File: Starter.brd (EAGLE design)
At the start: 44.1 x 26.7 mm, 9 parts, among them IC1 LM317MBSTT3

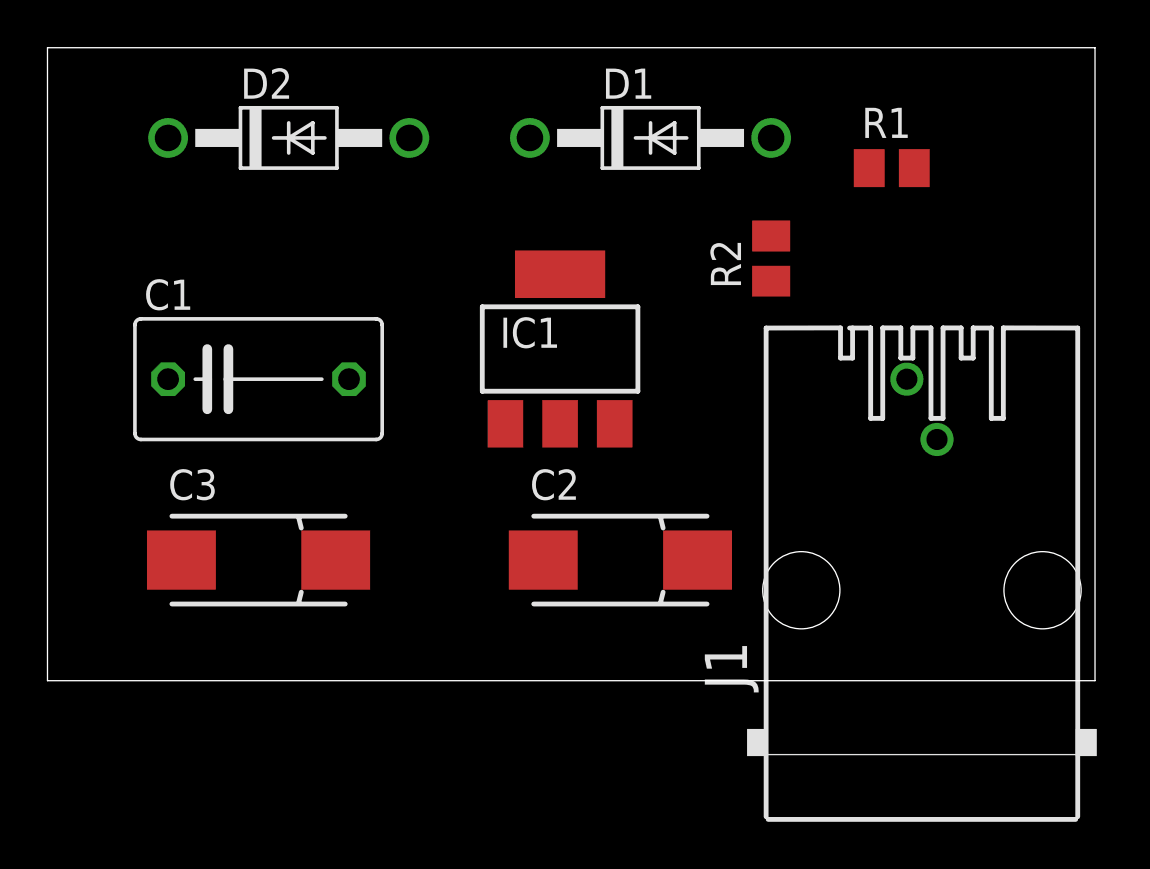
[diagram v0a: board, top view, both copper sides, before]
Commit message: Copper poured
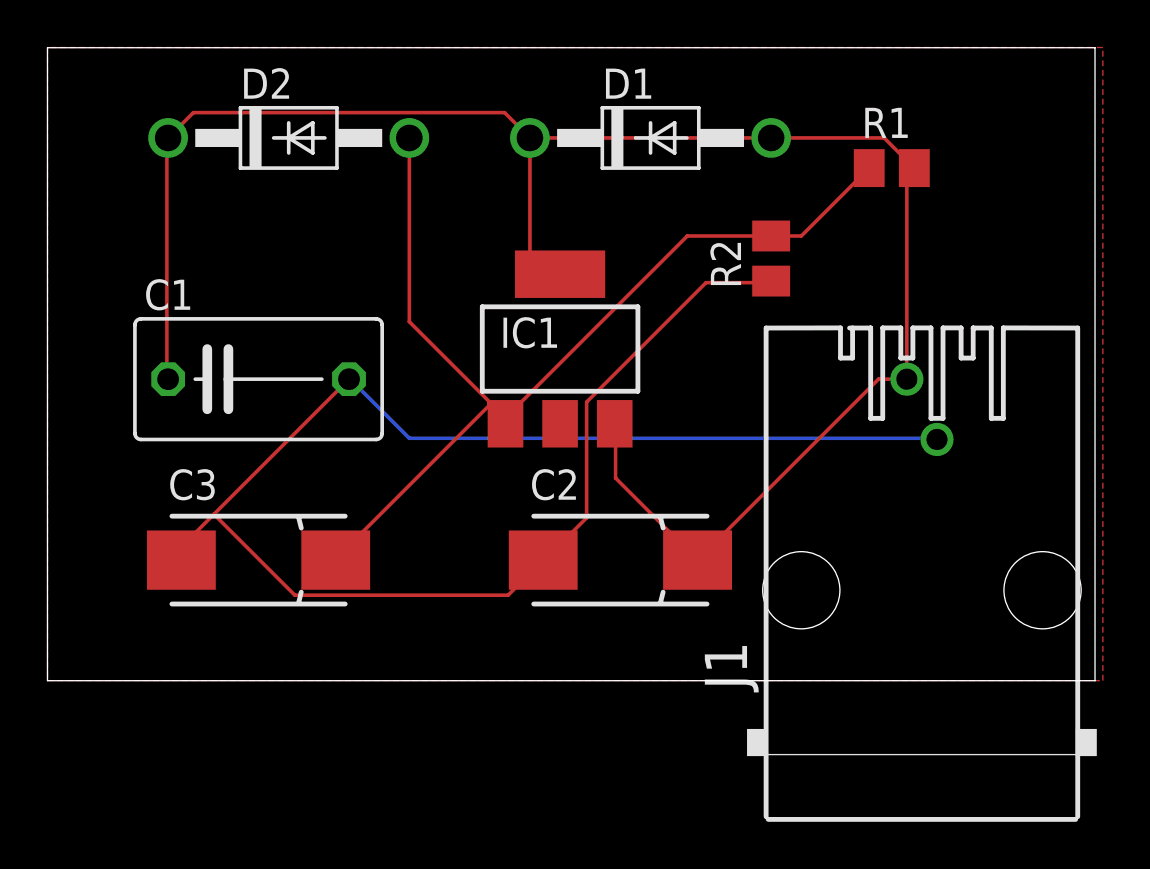
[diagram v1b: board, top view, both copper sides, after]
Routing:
- net +5V: track 0.00 -> 78.0 mm
- net GND: track 0.00 -> 69.6 mm
- net N$1: track 0.00 -> 43.9 mm
- added copper zone on layer 1, net GND
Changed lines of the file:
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@@
 <drawing>
 <settings>
-<setting alwaysvectorfont="no"/>
+<setting alwaysvectorfont="yes"/>
 <setting verticaltext="up"/>
 </settings>
@@
 <contactref element="C2" pad="-"/>
 <contactref element="J1" pad="2"/>
-<wire x1="20.88" y1="5.08" x2="30.48" y2="16.83" width="0" layer="19" extent="1-1"/>
-<wire x1="12.7" y1="12.7" x2="20.88" y2="5.08" width="0" layer="19" extent="1-1"/>
-<wire x1="5.64" y1="5.08" x2="12.7" y2="12.7" width="0" layer="19" extent="1-1"/>
-<wire x1="37.465" y1="10.16" x2="5.64" y2="5.08" width="0" layer="19" extent="1-1"/>
+<wire x1="27.7368" y1="16.764" x2="30.48" y2="16.764" width="0.1524" layer="1"/>
+<wire x1="22.7076" y1="11.7348" x2="27.7368" y2="16.764" width="0.1524" layer="1"/>
+<wire x1="22.7076" y1="6.858" x2="22.7076" y2="11.7348" width="0.1524" layer="1"/>
+<wire x1="21.0312" y1="5.1816" x2="22.7076" y2="6.858" width="0.1524" layer="1"/>
+<wire x1="30.48" y1="16.764" x2="30.48" y2="16.83" width="0.1524" layer="1"/>
+<wire x1="21.0312" y1="5.1816" x2="20.88" y2="5.08" width="0.1524" layer="1"/>
+<wire x1="15.24" y1="10.2108" x2="37.338" y2="10.2108" width="0.1524" layer="16"/>
+<wire x1="12.8016" y1="12.6492" x2="15.24" y2="10.2108" width="0.1524" layer="16"/>
+<wire x1="37.338" y1="10.2108" x2="37.465" y2="10.16" width="0.1524" layer="16"/>
+<wire x1="12.8016" y1="12.6492" x2="12.7" y2="12.7" width="0.1524" layer="16"/>
+<wire x1="5.7912" y1="5.7912" x2="5.7912" y2="5.1816" width="0.1524" layer="1"/>
+<wire x1="12.7" y1="12.7" x2="7.0104" y2="7.0104" width="0.1524" layer="1"/>
+<wire x1="7.0104" y1="7.0104" x2="5.7912" y2="5.7912" width="0.1524" layer="1"/>
+<wire x1="5.7912" y1="5.1816" x2="5.64" y2="5.08" width="0.1524" layer="1"/>
+<wire x1="7.0104" y1="7.0104" x2="10.4194" y2="3.6014" width="0.1524" layer="1"/>
+<wire x1="10.4194" y1="3.6014" x2="19.4014" y2="3.6014" width="0.1524" layer="1"/>
+<wire x1="19.4014" y1="3.6014" x2="20.88" y2="5.08" width="0.1524" layer="1"/>
+<polygon width="0.1524" layer="1">
+<vertex x="0" y="26.67"/>
+<vertex x="0" y="0"/>
+<vertex x="44.45" y="0"/>
+<vertex x="44.45" y="26.67"/>
+</polygon>
 </signal>
 <signal name="N$1">
@@
 <contactref element="R2" pad="2"/>
 <contactref element="C3" pad="+"/>
-<wire x1="30.48" y1="18.73" x2="34.61" y2="21.59" width="0" layer="19" extent="1-1"/>
-<wire x1="19.29" y1="10.82" x2="30.48" y2="18.73" width="0" layer="19" extent="1-1"/>
-<wire x1="12.14" y1="5.08" x2="19.29" y2="10.82" width="0" layer="19" extent="1-1"/>
-<wire x1="15.24" y1="22.86" x2="19.29" y2="10.82" width="0" layer="19" extent="1-1"/>
+<wire x1="30.48" y1="18.73" x2="26.95" y2="18.73" width="0.1524" layer="1"/>
+<wire x1="26.95" y1="18.73" x2="19.29" y2="11.07" width="0.1524" layer="1"/>
+<wire x1="15.24" y1="22.86" x2="15.24" y2="15.12" width="0.1524" layer="1"/>
+<wire x1="15.24" y1="15.12" x2="19.29" y2="11.07" width="0.1524" layer="1"/>
+<wire x1="19.29" y1="11.07" x2="19.29" y2="10.82" width="0.1524" layer="1"/>
+<wire x1="18.5928" y1="11.5824" x2="12.192" y2="5.1816" width="0.1524" layer="1"/>
+<wire x1="18.5928" y1="11.7348" x2="18.5928" y2="11.5824" width="0.1524" layer="1"/>
+<wire x1="12.192" y1="5.1816" x2="12.14" y2="5.08" width="0.1524" layer="1"/>
+<wire x1="18.5928" y1="11.7348" x2="19.29" y2="10.82" width="0.1524" layer="1"/>
+<wire x1="30.48" y1="18.73" x2="31.75" y2="18.73" width="0.1524" layer="1"/>
+<wire x1="31.75" y1="18.73" x2="34.61" y2="21.59" width="0.1524" layer="1"/>
 </signal>
 <signal name="+5V">
@@
 <contactref element="D1" pad="C"/>
 <contactref element="J1" pad="1"/>
-<wire x1="30.48" y1="22.86" x2="36.51" y2="21.59" width="0" layer="19" extent="1-1"/>
-<wire x1="20.32" y1="22.86" x2="30.48" y2="22.86" width="0" layer="19" extent="1-1"/>
-<wire x1="21.59" y1="17.12" x2="20.32" y2="22.86" width="0" layer="19" extent="1-1"/>
-<wire x1="23.89" y1="10.82" x2="21.59" y2="17.12" width="0" layer="19" extent="1-1"/>
-<wire x1="27.38" y1="5.08" x2="23.89" y2="10.82" width="0" layer="19" extent="1-1"/>
-<wire x1="5.08" y1="22.86" x2="20.32" y2="22.86" width="0" layer="19" extent="1-1"/>
-<wire x1="5.08" y1="12.7" x2="5.08" y2="22.86" width="0" layer="19" extent="1-1"/>
-<wire x1="36.195" y1="12.7" x2="5.08" y2="22.86" width="0" layer="19" extent="1-1"/>
+<wire x1="36.51" y1="21.59" x2="36.195" y2="21.275" width="0.1524" layer="1"/>
+<wire x1="36.195" y1="21.275" x2="36.195" y2="12.7" width="0.1524" layer="1"/>
+<wire x1="20.32" y1="22.86" x2="20.32" y2="17.49" width="0.1524" layer="1"/>
+<wire x1="20.32" y1="17.49" x2="20.69" y2="17.12" width="0.1524" layer="1"/>
+<wire x1="20.69" y1="17.12" x2="21.59" y2="17.12" width="0.1524" layer="1"/>
+<wire x1="20.32" y1="22.86" x2="19.2532" y2="23.9268" width="0.1524" layer="1"/>
+<wire x1="19.2532" y1="23.9268" x2="6.1468" y2="23.9268" width="0.1524" layer="1"/>
+<wire x1="6.1468" y1="23.9268" x2="5.08" y2="22.86" width="0.1524" layer="1"/>
+<wire x1="5.0292" y1="22.86" x2="5.0292" y2="12.8016" width="0.1524" layer="1"/>
+<wire x1="5.0292" y1="12.8016" x2="5.08" y2="12.7" width="0.1524" layer="1"/>
+<wire x1="5.0292" y1="22.86" x2="5.08" y2="22.86" width="0.1524" layer="1"/>
+<wire x1="23.9268" y1="8.5344" x2="23.9268" y2="10.668" width="0.1524" layer="1"/>
+<wire x1="27.2796" y1="5.1816" x2="23.9268" y2="8.5344" width="0.1524" layer="1"/>
+<wire x1="23.9268" y1="10.668" x2="23.89" y2="10.82" width="0.1524" layer="1"/>
+<wire x1="27.2796" y1="5.1816" x2="27.38" y2="5.08" width="0.1524" layer="1"/>
+<wire x1="30.48" y1="22.86" x2="20.32" y2="22.86" width="0.1524" layer="1"/>
+<wire x1="36.195" y1="12.7" x2="35" y2="12.7" width="0.1524" layer="1"/>
+<wire x1="35" y1="12.7" x2="27.38" y2="5.08" width="0.1524" layer="1"/>
+<wire x1="36.51" y1="21.59" x2="35.24" y2="22.86" width="0.1524" layer="1"/>
+<wire x1="35.24" y1="22.86" x2="30.48" y2="22.86" width="0.1524" layer="1"/>
 </signal>
 </signals>
